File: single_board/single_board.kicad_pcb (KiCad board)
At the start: 4 copper layers, 100 x 100 mm, 126 parts, among them J11 SPI Debug, J17 BOOTSEL, J2 USB_C_Receptacle_USB2.0_16P, J3 SWD, J30 JST_GH_H, J31 JST_GH_H, J33 JST_GH_H, J34 PB_Vertical, J35 JST_GH_H, J36 JST_GH_H, J37 JST_GH_H, J38 PB_Vertical, J39 PB_Vertical, J40 PB_Vertical, J41 PB_Vertical, J42 PB_Vertical, J43 PB_Vertical, J44 PB_Vertical, J45 PB_Vertical, J46 PB_Vertical, J47 PB_Vertical, J48 PB_Vertical, J49 PB_Vertical, J5 JST-GH, J50 PB_Vertical, J53 PB_Vertical, J55 PB_Vertical, J56 Power, J57 PB_Vertical, J6 JST-GH, Q1 AO3400A, Q3 AO3401A, SW1 Button, U1 AP2112K-3.3, U3 USBLC6-2SC6, U4 LSM6DSV, U5 STM32G474VBTx, Y2 ABM8-16MHz

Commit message: Copper Pours
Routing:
- net /RST: track 1.89 -> 53.2 mm, vias 1 -> 2
- net v3v3: track 21.4 -> 31.6 mm, vias 30 -> 35
- net Net-(R19-Pad1): track 0.00 -> 5.73 mm
- net /SWCLK: track 34.9 -> 35.5 mm, vias 0 -> 2
- net /SWDIO: track 36.5 -> 36.6 mm, vias 0 -> 2
- net GND: vias 103 -> 108
- added copper zone on B.Cu, net 5V
- added copper zone on B.Cu, net v3v3

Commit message: Front Silkscreen
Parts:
- moved D12 7.00 mm to (132.8, 40.5)
- moved D9 7.00 mm to (132.8, 32.6)
- moved D10 7.00 mm to (132.8, 35.2)
- moved D11 7.00 mm to (132.8, 37.9)
- moved D15 7.00 mm to (132.8, 43.1)
- moved D8 7.00 mm to (132.8, 30.0)
- moved R11 7.00 mm to (129.4, 30.0)
- moved R12 7.00 mm to (129.4, 32.6)
- moved R13 7.00 mm to (129.4, 35.2)
- moved R16 7.00 mm to (129.4, 37.9)
- moved R17 7.00 mm to (129.4, 40.5)
- moved R20 7.00 mm to (129.4, 43.1)
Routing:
- net /LED6: track 29.4 -> 36.1 mm
- net /LED5: track 37.8 -> 44.0 mm
- net /LED2: track 51.3 -> 57.5 mm
- net /LED4: track 38.5 -> 44.7 mm
- net /LED3: track 47.1 -> 53.3 mm
- net /LED1: track 44.3 -> 49.8 mm
- net /USART3_TX: track 50.7 -> 53.9 mm
- net /USART3_RX: track 50.0 -> 53.2 mm
- net /SPI2_SCK: track 44.5 -> 43.6 mm
- net /SPI2_MISO: track 43.9 -> 43.3 mm
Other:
- board text added: "Rover Control Board V1"
- board text added: "X"
- board text added: "Y"
- board text added: "Z"

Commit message: Back Silkscreen
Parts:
- added G***: LOGO, LOGO, F.Cu at (102.2, 77.4)
- added G***: LOGO, Mathai_E_Libs:sss-logo, B.Cu at (97.8, 63.9)
- added G***: LOGO, LOGO, B.Cu at (131.3, 97.2)
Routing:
- net Net-(J56-Pin_2): track 5.09 -> 10.2 mm, vias 1 -> 0
- net Net-(D1-A): track 0.00 -> 2.20 mm
- net Net-(D15-A): track 0.00 -> 2.02 mm
- net Net-(D12-A): track 0.00 -> 2.02 mm
- net Net-(D11-A): track 0.00 -> 2.02 mm
- net Net-(D10-A): track 0.00 -> 2.02 mm
- net Net-(D9-A): track 0.00 -> 2.02 mm
- net Net-(D8-A): track 0.00 -> 2.02 mm
- net Net-(D13-A): track 0.00 -> 1.66 mm
- net Net-(D14-A): track 0.00 -> 1.65 mm
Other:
- board text added: "RC 2026 - ELEC CONTROLS EJ dela Cruz EM AD"

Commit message: Stitching Vias
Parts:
- moved G*** 2.33 mm to (133.6, 97.1)
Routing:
- net v3v3: vias 35 -> 47
- net GND: vias 108 -> 681
- net 5V: vias 4 -> 14
- net /LIM_SW1: vias 0 -> 1
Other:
- board text added: "1.1"
- board text added: "3 1 1.8"

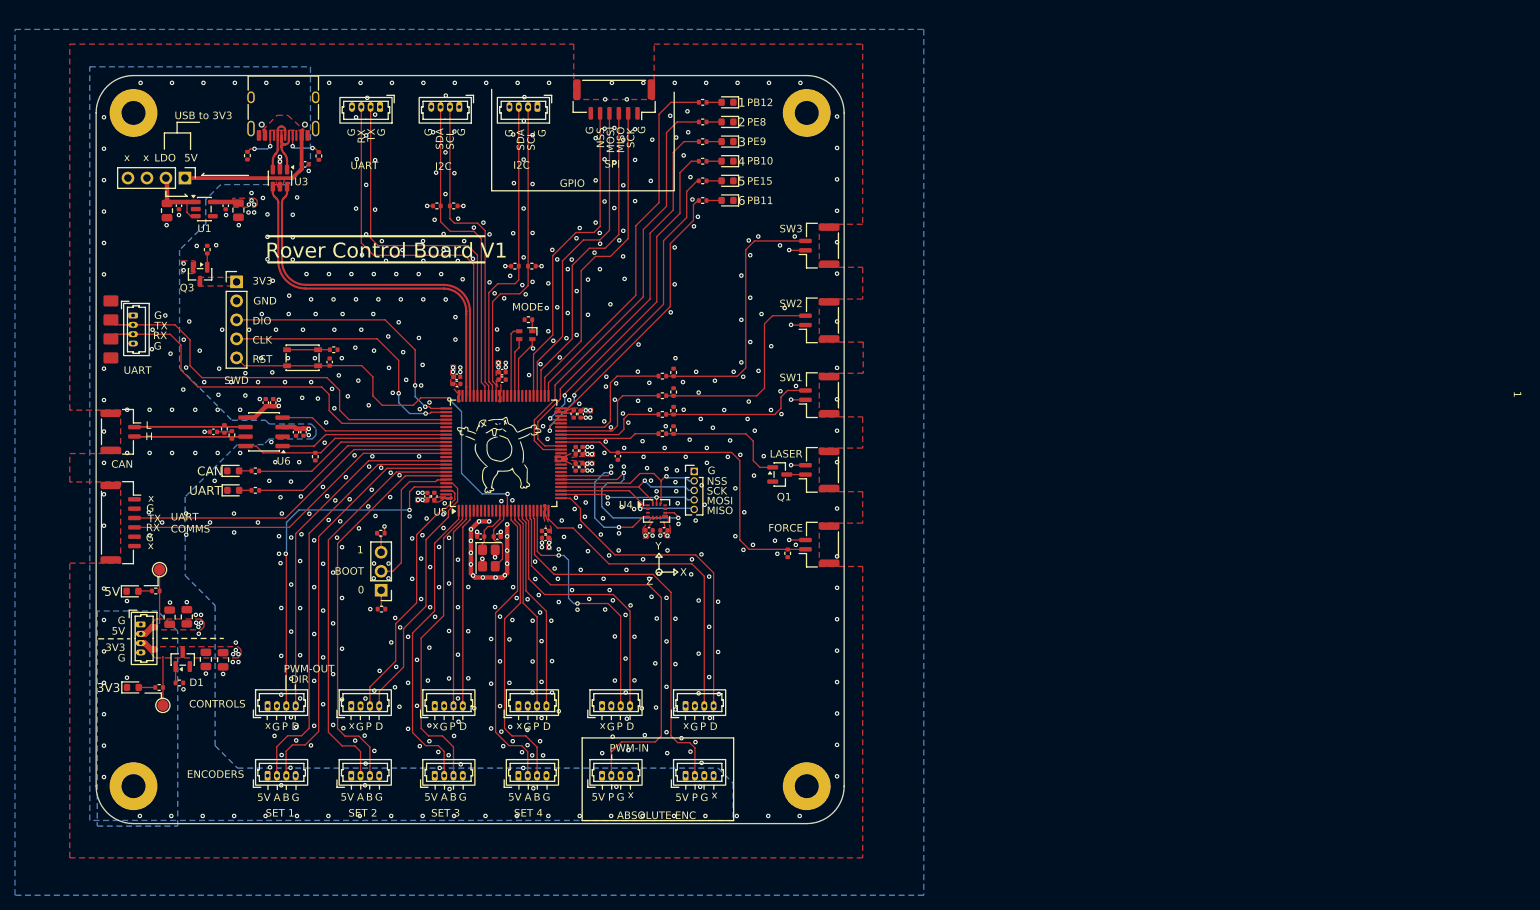
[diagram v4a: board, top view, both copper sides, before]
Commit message: More Stitching Vias
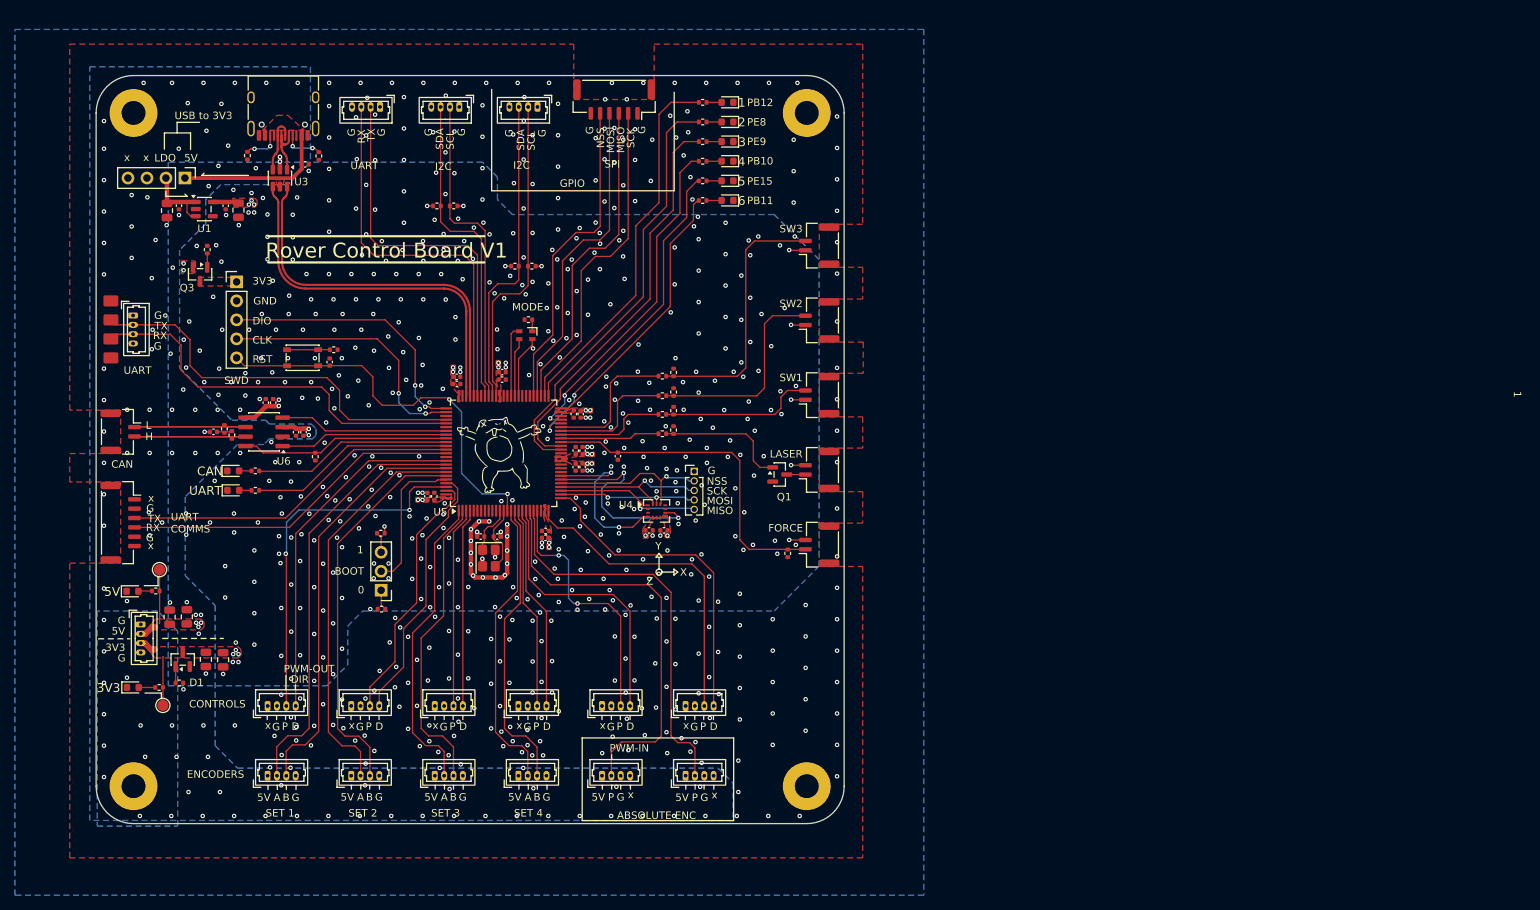
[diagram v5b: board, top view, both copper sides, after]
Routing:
- net v3v3: vias 47 -> 35
- net unconnected-(H1-Pad1): vias 0 -> 1
- net GND: vias 681 -> 785
- net 5V: vias 14 -> 4
